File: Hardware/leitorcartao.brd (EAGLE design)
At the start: 34.5 x 56.7 mm, 156 parts, among them IC1 TL084, IC2 TL084, Q1 DMN3404, Q4 BC847ALT1SMD, Q5 BC847ALT1SMD, Q6 BC847ALT1SMD, Q7 BC847ALT1SMD, Q8 MMBT4403, Q9 MMBT4401, U1 SAMD20E14A-AUT, U3 TLV1117-50CDCYR, U4 MFRC52202HN1, U5 LP2985-33DBVR, X1 ANTENA, X2 MIFARE ANTENA

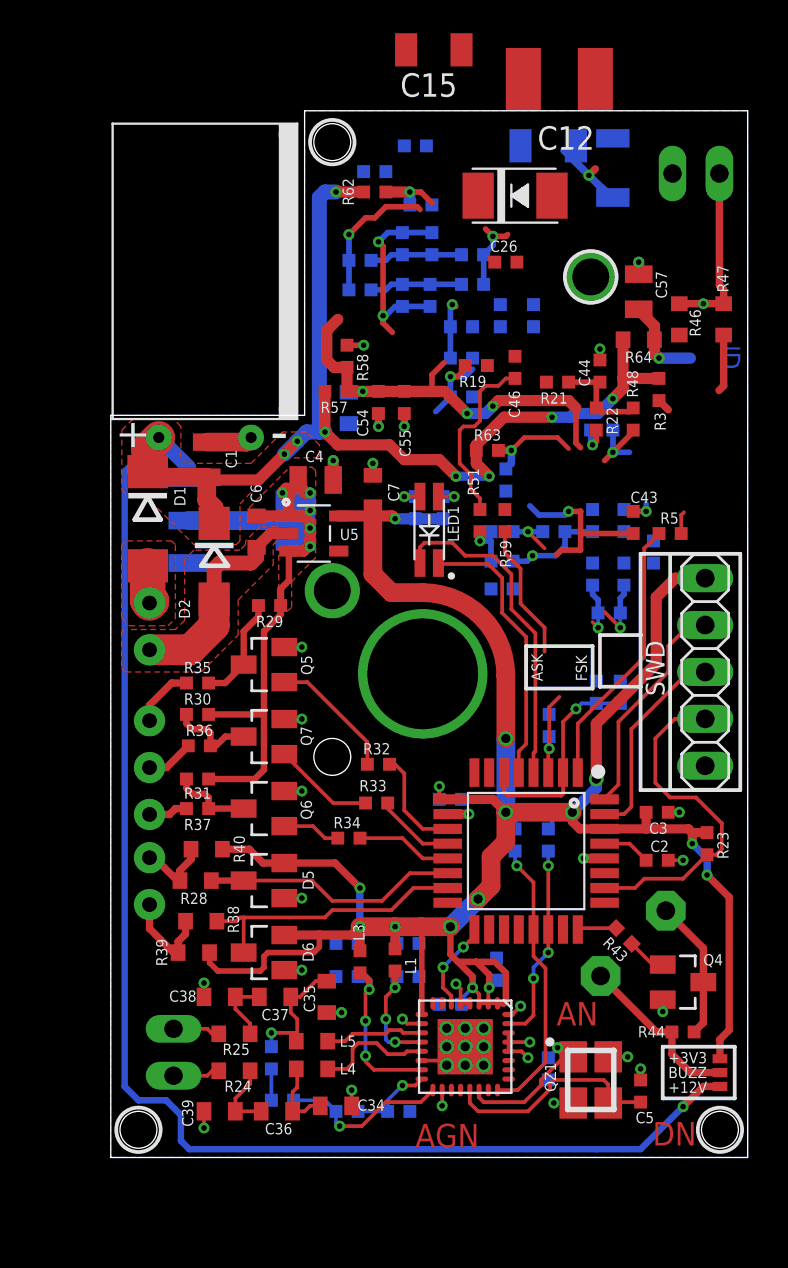
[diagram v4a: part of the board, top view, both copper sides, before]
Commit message: Adicionadas duas novas camadas na placa.
Layer 4 -> Power Plane
Layer 5 -> Ground Plane
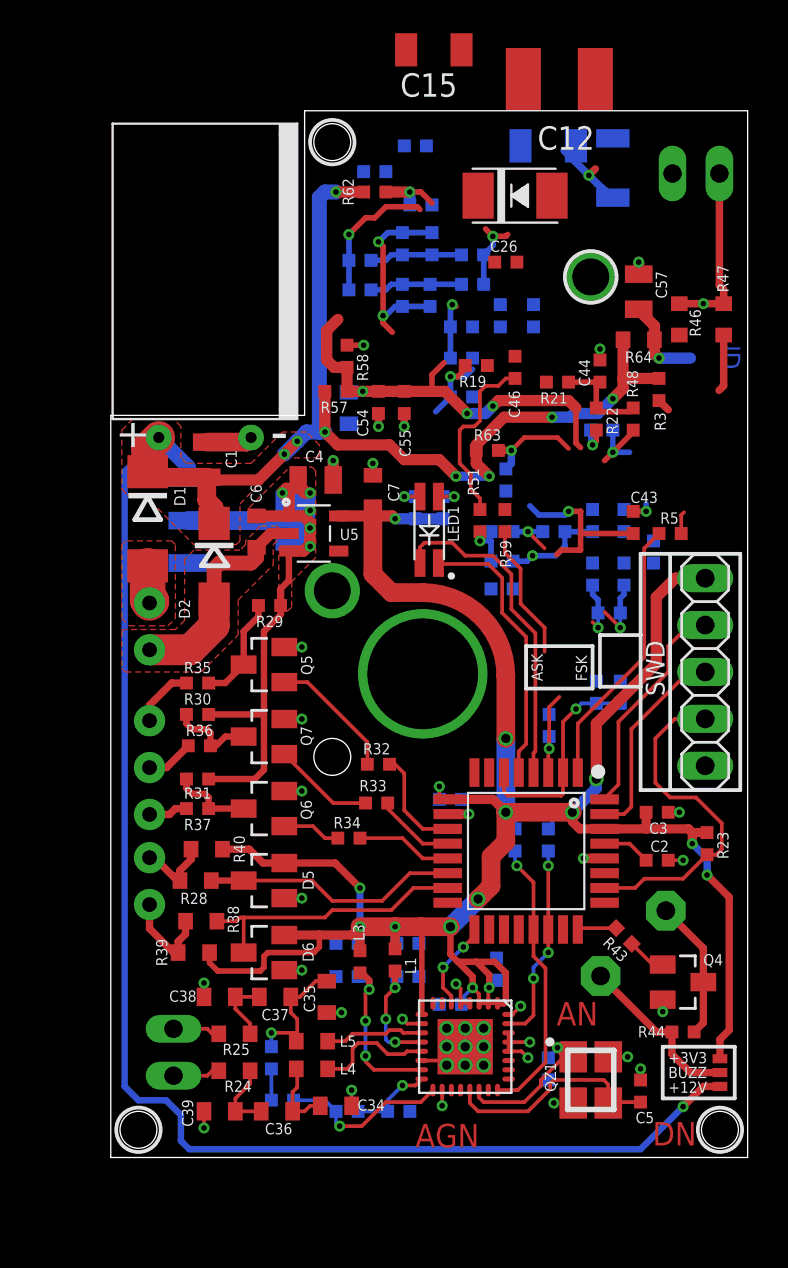
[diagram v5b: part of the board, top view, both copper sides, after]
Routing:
- added copper zone on layer 5, net GND
- removed copper zone on layer 16, net GND
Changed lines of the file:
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@@
 <layer number="2" name="Route2" color="1" fill="3" visible="no" active="no"/>
 <layer number="3" name="Route3" color="4" fill="3" visible="no" active="no"/>
-<layer number="4" name="Route4" color="1" fill="4" visible="no" active="no"/>
-<layer number="5" name="Route5" color="4" fill="4" visible="no" active="no"/>
+<layer number="4" name="Route4" color="11" fill="1" visible="yes" active="yes"/>
+<layer number="5" name="Route5" color="13" fill="1" visible="no" active="yes"/>
 <layer number="6" name="Route6" color="1" fill="8" visible="no" active="no"/>
 <layer number="7" name="Route7" color="4" fill="8" visible="no" active="no"/>
@@
 </class>
 </classes>
-<designrules name="Fusion_eagle_rule_v1.1">
+<designrules name="Fusion_eagle_rule_v1.1 *">
 <description language="de">&lt;b&gt;EAGLE Design Rules&lt;/b&gt;
 &lt;p&gt;
@@
 <description language="zh">&lt;b&gt;Seeed Studio EAGLE Design Rules&lt;/b&gt;
 </description>
-<param name="layerSetup" value="(1*16)"/>
+<param name="layerSetup" value="(1+4*5+16)"/>
 <param name="mtCopper" value="0.035mm 0.035mm 0.035mm 0.035mm 0.035mm 0.035mm 0.035mm 0.035mm 0.035mm 0.035mm 0.035mm 0.035mm 0.035mm 0.035mm 0.035mm 0.035mm"/>
-<param name="mtIsolate" value="1.5mm 0.15mm 0.2mm 0.15mm 0.2mm 0.15mm 0.2mm 0.15mm 0.2mm 0.15mm 0.2mm 0.15mm 0.2mm 0.15mm 0.2mm"/>
+<param name="mtIsolate" value="0.2mm 0.15mm 0.2mm 1.1mm 0.2mm 0.15mm 0.2mm 0.15mm 0.2mm 0.15mm 0.2mm 0.15mm 0.2mm 0.15mm 0.2mm"/>
 <param name="mdWireWire" value="8mil"/>
 <param name="mdWirePad" value="8mil"/>
@@
 <contactref element="C25" pad="2"/>
 <contactref element="C44" pad="2"/>
-<polygon width="0.2032" layer="16">
-<vertex x="0" y="0"/>
-<vertex x="34.5" y="0"/>
-<vertex x="34.5" y="56.7"/>
-<vertex x="10.5" y="56.7"/>
-<vertex x="10.5" y="40.2"/>
-<vertex x="0" y="40.2"/>
-</polygon>
 <contactref element="U5" pad="2"/>
 <wire x1="5.2" y1="38.75" x2="7.35" y2="38.75" width="1.016" layer="1"/>
@@
 <contactref element="IC1" pad="11"/>
 <contactref element="IC2" pad="11"/>
+<polygon width="0.127" layer="5">
+<vertex x="0" y="0"/>
+<vertex x="34.5" y="0"/>
+<vertex x="34.5" y="56.7"/>
+<vertex x="10.5" y="56.7"/>
+<vertex x="10.5" y="40.2"/>
+<vertex x="0" y="40.2"/>
+<vertex x="0" y="39.5"/>
+</polygon>
 <wire x1="-31.95" y1="-57.5" x2="-32.9" y2="-65.8" width="0" layer="19" extent="1-1"/>
 <wire x1="-32.4" y1="-46.2" x2="-31.95" y2="-57.5" width="0" layer="19" extent="1-1"/>
@@
 <wire x1="-26.8" y1="-22.3" x2="-27.9" y2="-45.5" width="0" layer="19" extent="1-1"/>
 <wire x1="5.05" y1="1.6" x2="-26.8" y2="-22.3" width="0" layer="19" extent="1-1"/>
-<wire x1="5.05" y1="8.7" x2="5.05" y2="2.5" width="0" layer="19" extent="1-1"/>
-<wire x1="9.4" y1="10.15" x2="5.05" y2="9.45" width="0" layer="19" extent="1-1"/>
-<wire x1="12.2" y1="9.8" x2="10.35" y2="10.15" width="0" layer="19" extent="16-16"/>
-<wire x1="12.2" y1="11.6" x2="12.2" y2="9.8" width="0" layer="19" extent="16-16"/>
-<wire x1="12.5" y1="7.85" x2="12.2" y2="9.8" width="0" layer="19" extent="1-16"/>
-<wire x1="10.35" y1="14.05" x2="12.2" y2="11.6" width="0" layer="19" extent="16-16"/>
-<wire x1="15.8" y1="7.5" x2="12.5" y2="7.85" width="0" layer="19" extent="1-1"/>
-<wire x1="18.2" y1="7" x2="16.85" y2="7.25" width="0" layer="19" extent="1-1"/>
-<wire x1="18.2" y1="6" x2="18.2" y2="7" width="0" layer="19" extent="1-1"/>
-<wire x1="17.95" y1="5.25" x2="18.2" y2="6" width="0" layer="19" extent="1-1"/>
-<wire x1="19.2" y1="6" x2="18.2" y2="6" width="0" layer="19" extent="1-1"/>
-<wire x1="20.2" y1="6" x2="19.2" y2="6" width="0" layer="19" extent="1-1"/>
-<wire x1="20.2" y1="7" x2="20.2" y2="6" width="0" layer="19" extent="1-1"/>
-<wire x1="19.2" y1="7" x2="18.2" y2="7" width="0" layer="19" extent="1-1"/>
-<wire x1="19.2" y1="5" x2="18.2" y2="5" width="0" layer="19" extent="1-1"/>
-<wire x1="20.2" y1="5" x2="20.2" y2="6" width="0" layer="19" extent="1-1"/>
-<wire x1="17.8" y1="8.3" x2="18.2" y2="7" width="0" layer="19" extent="16-16"/>
-<wire x1="18.95" y1="8.35" x2="17.8" y2="8.3" width="0" layer="19" extent="1-16"/>
-<wire x1="21.55" y1="5.75" x2="20.2" y2="6" width="0" layer="19" extent="1-1"/>
-<wire x1="21.55" y1="7.75" x2="21.55" y2="6.75" width="0" layer="19" extent="1-1"/>
-<wire x1="17.95" y1="3.65" x2="18.2" y2="5" width="0" layer="19" extent="1-1"/>
-<wire x1="23.7" y1="4.2" x2="22.6" y2="5.4" width="0" layer="19" extent="16-16"/>
-<wire x1="24" y1="2.95" x2="23.7" y2="4.2" width="0" layer="19" extent="1-16"/>
+<wire x1="19" y1="19.4" x2="19.4" y2="18.6" width="0" layer="19" extent="1-16"/>
+<wire x1="17.8" y1="8.3" x2="18.95" y2="8.35" width="0" layer="19" extent="1-16"/>
+<wire x1="23.7" y1="4.2" x2="24" y2="2.95" width="0" layer="19" extent="1-16"/>
+<wire x1="4.2" y1="32.2" x2="5.6" y2="31.9" width="0" layer="19" extent="1-16"/>
+<wire x1="12.9" y1="39.75" x2="14.5" y2="39.6" width="0" layer="19" extent="1-16"/>
 <wire x1="16.2" y1="2.5" x2="17.95" y2="2.8" width="0" layer="19" extent="1-16"/>
 <wire x1="16.7" y1="9.8" x2="17.8" y2="8.3" width="0" layer="19" extent="16-16"/>
 <wire x1="16.7" y1="11.6" x2="16.7" y2="9.8" width="0" layer="19" extent="16-16"/>
+<wire x1="12.2" y1="9.8" x2="10.35" y2="10.15" width="0" layer="19" extent="16-16"/>
+<wire x1="12.2" y1="11.6" x2="12.2" y2="9.8" width="0" layer="19" extent="16-16"/>
 <wire x1="20.9" y1="10.8" x2="18.95" y2="9.15" width="0" layer="19" extent="1-16"/>
-<wire x1="26.95" y1="5.45" x2="25.05" y2="2.95" width="0" layer="19" extent="1-1"/>
-<wire x1="28.7" y1="4.8" x2="28" y2="5.45" width="0" layer="19" extent="1-1"/>
-<wire x1="29.9" y1="7.9" x2="28" y2="5.45" width="0" layer="19" extent="1-1"/>
-<wire x1="13.05" y1="2.8" x2="16.2" y2="2.5" width="0" layer="19" extent="1-16"/>
-<wire x1="10.35" y1="19.85" x2="10.35" y2="14.05" width="0" layer="19" extent="1-1"/>
-<wire x1="10.35" y1="23.75" x2="10.35" y2="19.85" width="0" layer="19" extent="1-1"/>
-<wire x1="10.35" y1="27.65" x2="10.35" y2="23.75" width="0" layer="19" extent="1-1"/>
-<wire x1="12" y1="30.7" x2="10.35" y2="27.65" width="0" layer="19" extent="1-1"/>
-<wire x1="9.65" y1="33.8" x2="12" y2="30.7" width="0" layer="19" extent="1-1"/>
-<wire x1="4.2" y1="32.2" x2="5.6" y2="31.9" width="0" layer="19" extent="1-16"/>
-<wire x1="12.05" y1="36.7" x2="9.65" y2="33.8" width="0" layer="19" extent="1-1"/>
-<wire x1="12.9" y1="39.75" x2="12.05" y2="37.75" width="0" layer="19" extent="1-16"/>
-<wire x1="14.5" y1="39.6" x2="12.9" y2="39.75" width="0" layer="19" extent="1-16"/>
-<wire x1="15.9" y1="40.3" x2="14.5" y2="40.3" width="0" layer="19" extent="1-1"/>
-<wire x1="14.2" y1="37.6" x2="14.5" y2="39.6" width="0" layer="19" extent="1-1"/>
-<wire x1="13.7" y1="44" x2="14.5" y2="40.3" width="0" layer="19" extent="1-1"/>
-<wire x1="7.6" y1="39" x2="12.05" y2="37.75" width="0" layer="19" extent="1-1"/>
+<wire x1="21.1" y1="46.2" x2="26" y2="47.7" width="0" layer="19" extent="16-16"/>
 <wire x1="21.4" y1="36.1" x2="15.9" y2="39.6" width="0" layer="19" extent="1-16"/>
-<wire x1="16.9" y1="26.2" x2="12" y2="30.7" width="0" layer="19" extent="1-1"/>
-<wire x1="28.3" y1="35" x2="21.4" y2="36.1" width="0" layer="19" extent="1-16"/>
-<wire x1="19" y1="19.4" x2="16.9" y2="26.2" width="0" layer="19" extent="16-16"/>
-<wire x1="19.4" y1="18.6" x2="19" y2="19.4" width="0" layer="19" extent="1-16"/>
-<wire x1="23.75" y1="24" x2="19" y2="19.4" width="0" layer="19" extent="16-16"/>
-<wire x1="26.3" y1="25.8" x2="23.75" y2="24" width="0" layer="19" extent="16-16"/>
-<wire x1="25.6" y1="16.2" x2="19.4" y2="18.6" width="0" layer="19" extent="1-1"/>
-<wire x1="30.2" y1="16.1" x2="26.75" y2="16.2" width="0" layer="19" extent="1-1"/>
-<wire x1="30.8" y1="18.7" x2="31" y2="16.1" width="0" layer="19" extent="1-1"/>
-<wire x1="32.2" y1="21.22" x2="30.8" y2="18.7" width="0" layer="19" extent="1-1"/>
-<wire x1="21.1" y1="46.2" x2="13.7" y2="44" width="0" layer="19" extent="1-16"/>
-<wire x1="26" y1="47.7" x2="21.1" y2="46.2" width="0" layer="19" extent="16-16"/>
-<wire x1="28.6" y1="47.85" x2="26" y2="47.7" width="0" layer="19" extent="1-1"/>
-<wire x1="26.5" y1="43.8" x2="26" y2="47.7" width="0" layer="19" extent="1-1"/>
 <wire x1="17.4" y1="51.6" x2="21.1" y2="46.2" width="0" layer="19" extent="16-16"/>
 <wire x1="13.7" y1="53.4" x2="17.4" y2="51.6" width="0" layer="19" extent="16-16"/>
@@
 <wire x1="22.35" y1="58.4" x2="22.2" y2="54.8" width="0" layer="19" extent="1-16"/>
 <wire x1="27.2" y1="55.2" x2="22.2" y2="54.8" width="0" layer="19" extent="16-16"/>
+<wire x1="23.75" y1="24" x2="19" y2="19.4" width="0" layer="19" extent="16-16"/>
+<wire x1="26.3" y1="25.8" x2="23.75" y2="24" width="0" layer="19" extent="16-16"/>
 </signal>
 <signal name="+3V3">

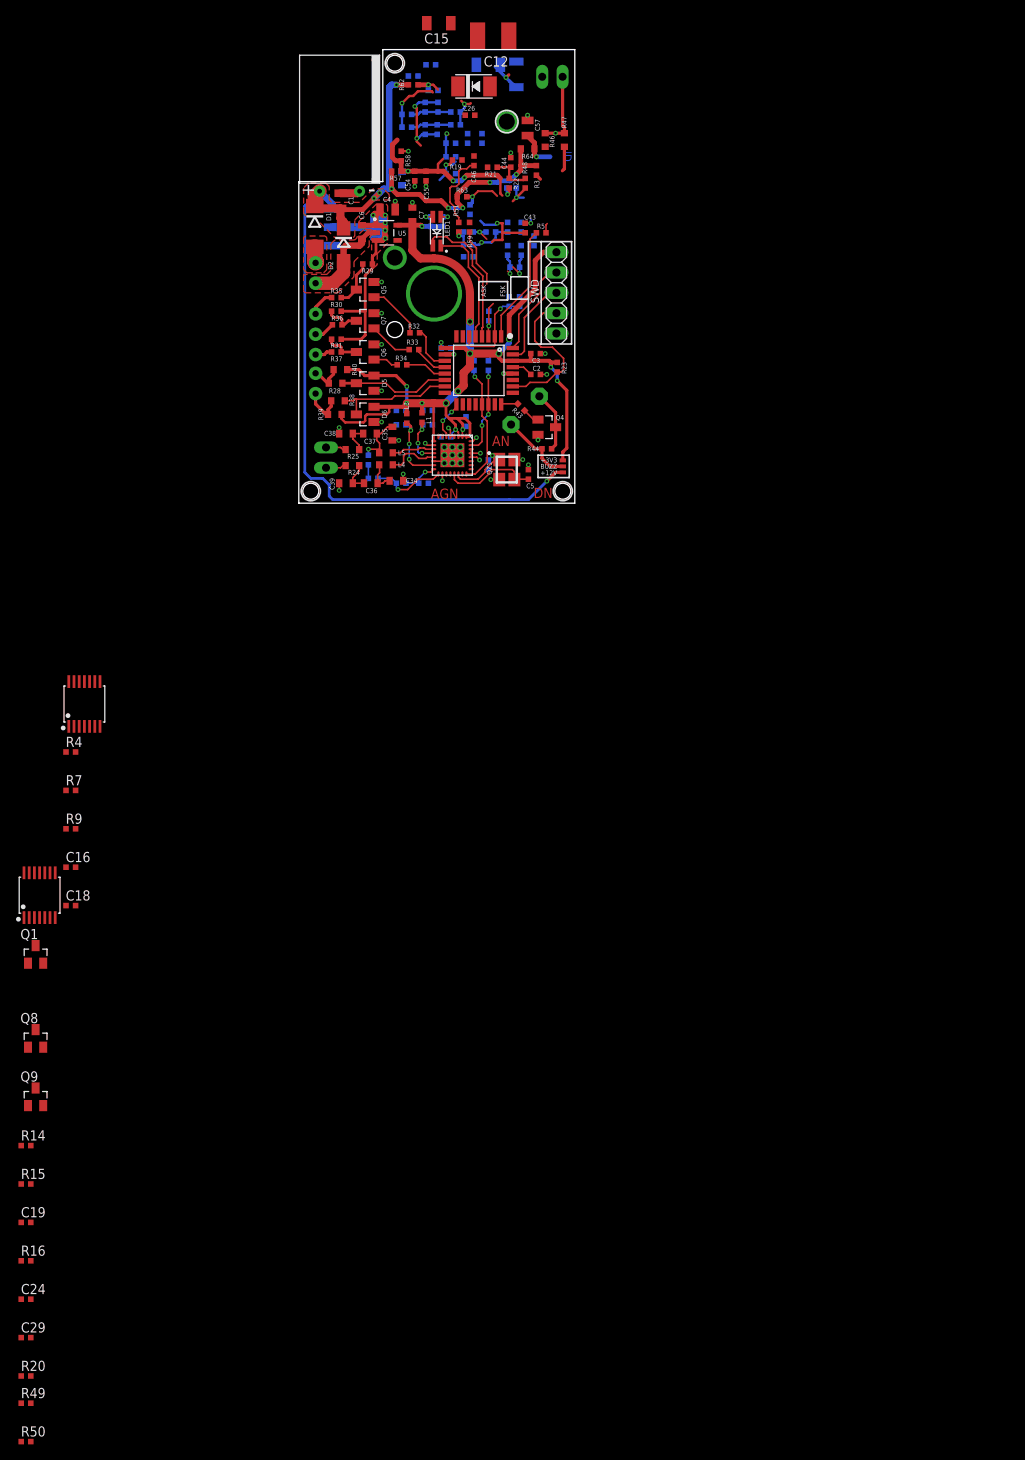
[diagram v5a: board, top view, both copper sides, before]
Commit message: Mudanças na placa.
Inclusão do LED Red/Green.
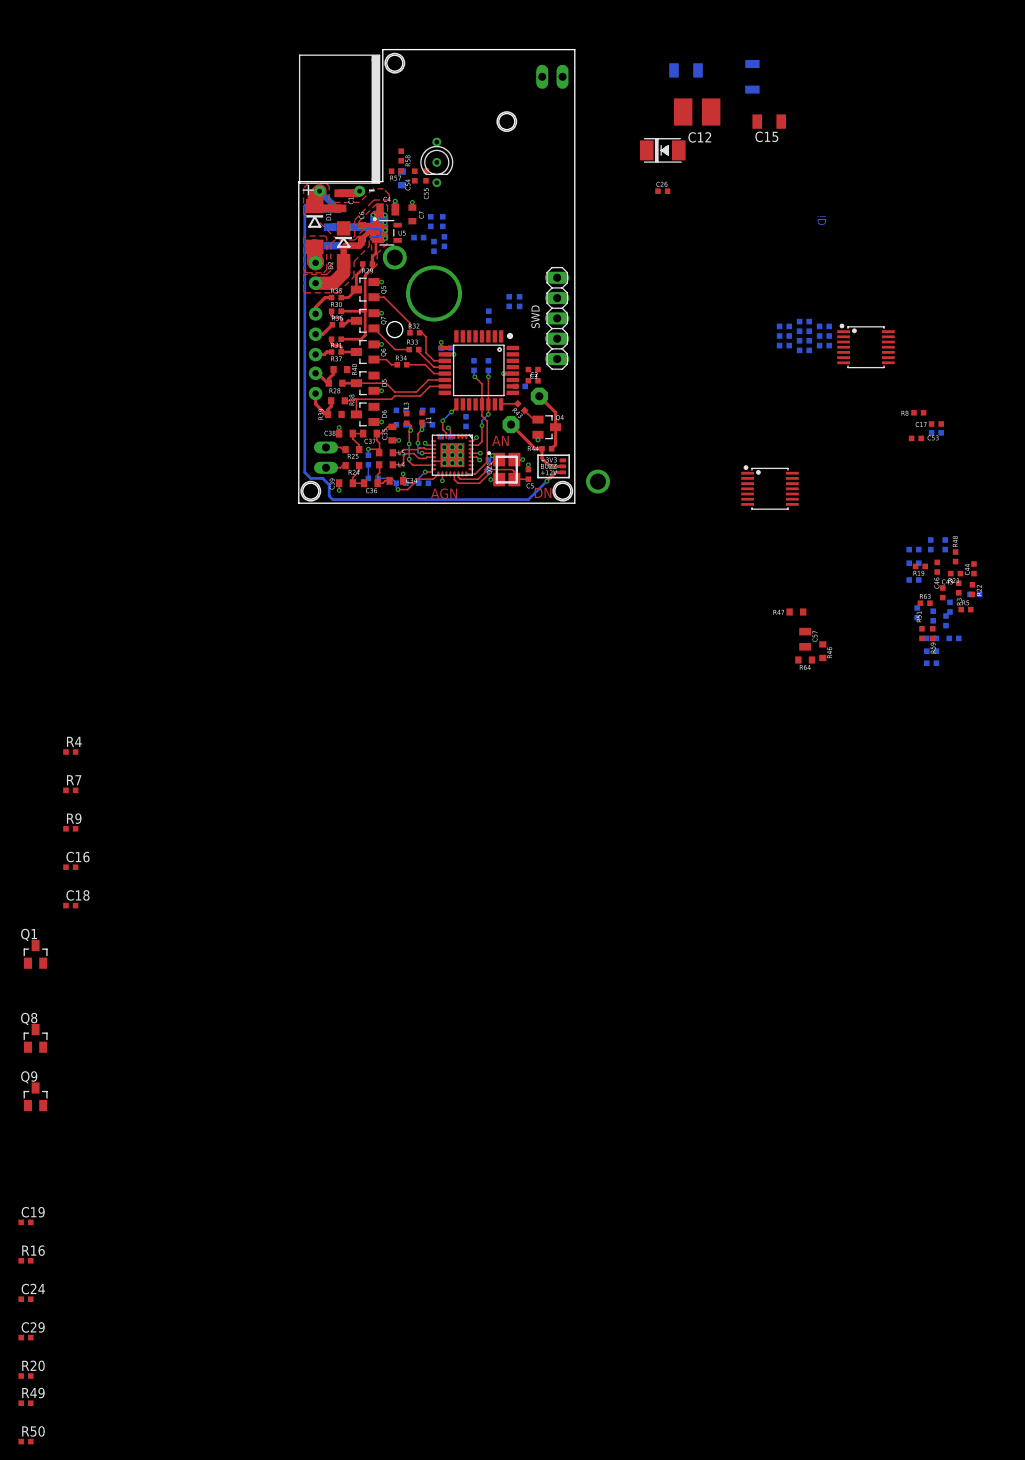
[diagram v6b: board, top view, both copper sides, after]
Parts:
- removed LED1: LTST-C235KGKRKT, RFiD:LTST-C235KGKRKT
- added LED2: LTL1BEKVJNN, RFiD:LTL1BEKVJNN
- R14: value 470k -> 470
- moved R15 145.6 mm to (65.7, 20.9), flipped to the bottom
- moved R14 138.7 mm to (60.7, 20.9), flipped to the bottom
- moved IC2 123.9 mm to (70.9, 19.5), turned to 270 degrees
- moved IC1 89.8 mm to (58.9, 1.80), turned to 270 degrees
- moved C17 78.5 mm to (79.7, 9.90), flipped to the top
- moved R62 78.5 mm to (79.7, 8.80), flipped to the bottom
- moved C28 77.0 mm to (76.9, -9.60)
- moved C25 77.0 mm to (79.0, -5.20)
- moved C27 77.0 mm to (76.9, -7.50)
- moved C44 77.0 mm to (84.4, -8.20)
- moved C45 77.0 mm to (84.5, -11.4)
- moved C46 77.0 mm to (79.8, -8.00)
- moved C47 77.0 mm to (79.1, -16.9)
- moved C48 77.0 mm to (79.1, -18.5)
- moved C52 77.0 mm to (79.3, -14.1)
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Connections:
- net +3V3: no longer R41.1, R42.2
- net GND: now also LED2.COMMON
- net LED-GREEN-CTRL: now also R41.1; no longer LED1.1
- net LED-RED-CTRL: now also R42.2; no longer LED1.4
- net N$52: now also LED2.ANODE_RED; no longer LED1.3
- net N$53: now also LED2.ANODE_GRN; no longer LED1.2
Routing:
- net +3V3: track 136.3 -> 2.85 mm, vias 15 -> 1
- net +12V: track 134.7 -> 80.4 mm, vias 9 -> 1
- net V+: track 32.6 -> 0.00 mm, vias 4 -> 0
- net RESET: track 18.7 -> 0.00 mm
- net LED-RED-CTRL: track 17.9 -> 0.00 mm
- net LED-GREEN-CTRL: track 15.1 -> 0.00 mm
- net 125KHZ-ANTENA: track 14.8 -> 0.00 mm
- net ASK-FSK: track 12.4 -> 0.00 mm, vias 1 -> 0
- net SWDIO: track 12.2 -> 0.00 mm
- net PSK: track 11.8 -> 0.00 mm, vias 1 -> 0
- net SWDCLK: track 11.1 -> 0.00 mm
- net N$17: track 11.1 -> 0.00 mm, vias 2 -> 0
- net N$69: track 9.85 -> 0.00 mm
- net N$11: track 9.55 -> 0.00 mm, vias 1 -> 0
- net N$23: track 7.53 -> 0.00 mm, vias 1 -> 0
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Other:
- board text removed: "ASK"
- board text removed: "FSK"
